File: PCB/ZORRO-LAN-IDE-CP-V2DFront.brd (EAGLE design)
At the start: 29 x 34.5 mm, 2 parts, among them X1 SI-50170

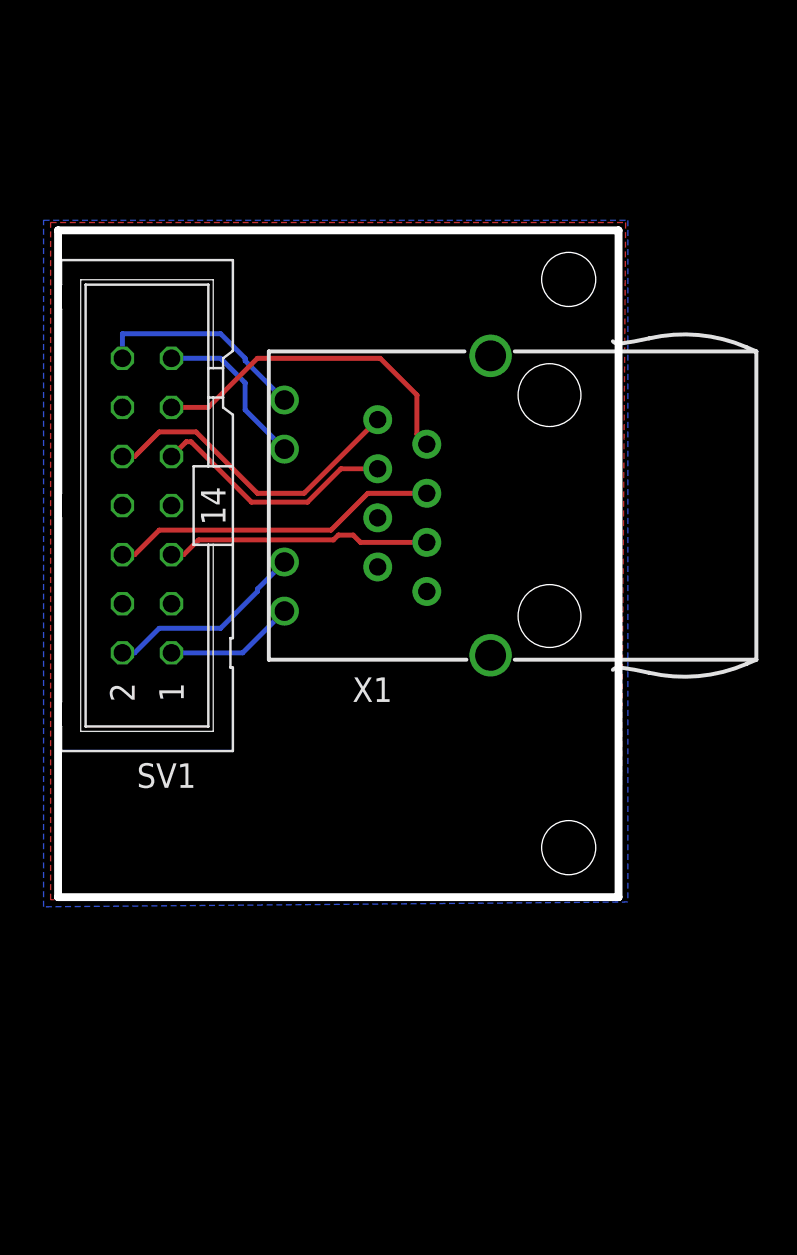
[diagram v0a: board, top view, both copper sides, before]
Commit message: Gerbers added and Front enlarged
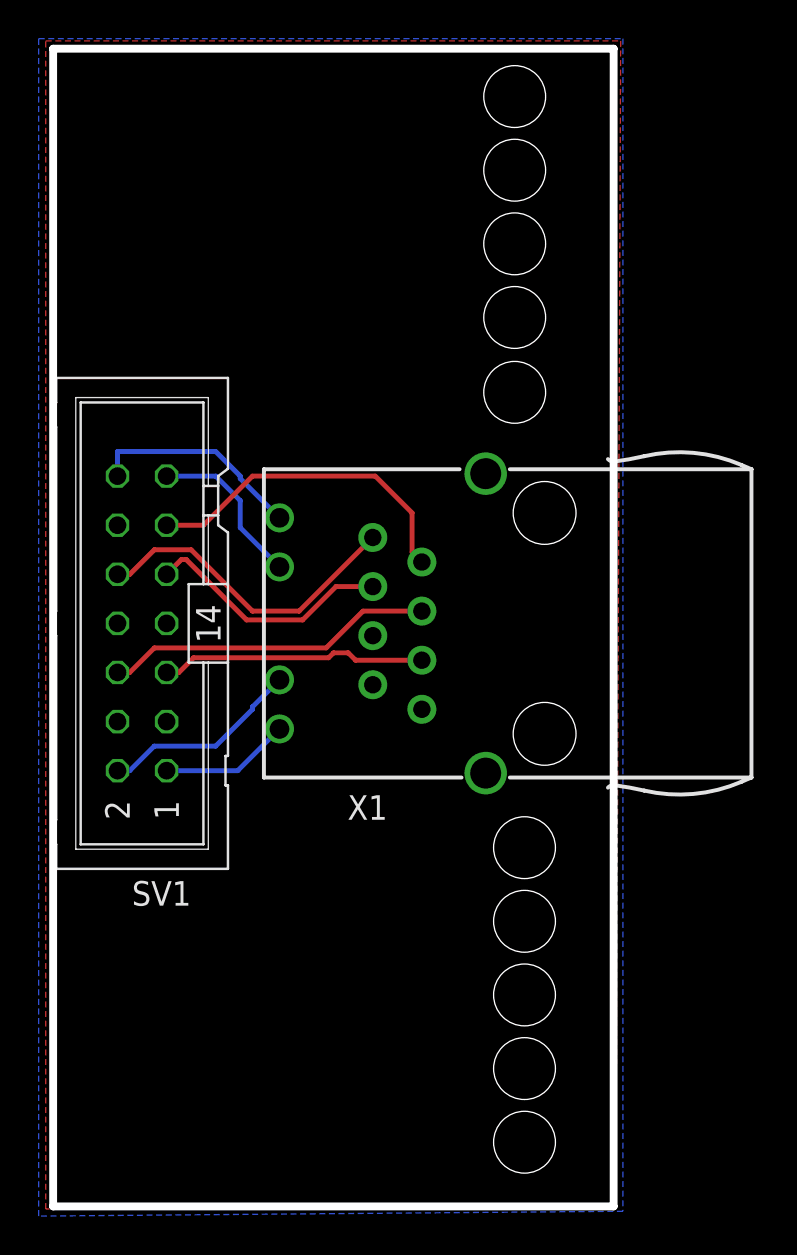
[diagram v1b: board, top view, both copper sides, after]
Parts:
- moved SV1 6.10 mm to (6.10, 10.4)
- moved X1 6.10 mm to (23.9, 10.4)
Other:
- board size 29 x 34.5 mm -> 29 x 59.9 mm
